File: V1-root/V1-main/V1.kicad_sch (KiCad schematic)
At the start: 214 parts, among them J17 OLED, Q1 PMOS, SW1 SW_SPST, U1 AP64500SP-3.3v, U7 XIAO-ESP32-S3-DIP_ui, Y1 Crystal_GND24

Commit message: 回路図とフットプリント終わった
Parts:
- removed J?: debug_STM, symbol Connector:Conn_01x09_Socket
- added J3: DebugSTM, Connector_PinSocket_2.54mm:PinSocket_1x07_P2.54mm_Vertical, symbol Connector:Conn_01x07_Socket
- BZ1: renamed from BZ?; footprint (none) -> Buzzer_Beeper:Buzzer_Murata_PKLCS1212E
- C1: footprint 74th:Capacitor_0402_1005 -> Capacitor_SMD:C_0603_1608Metric_Pad1.08x0.95mm_HandSolder
- C12, C18: renamed from C?; value C -> 4.7; footprint (none) -> Capacitor_SMD:C_0805_2012Metric_Pad1.18x1.45mm_HandSolder
- C13, C14, C15, C16, C17, C19, C20, C21, C22, C24, C25: renamed from C?; value C -> 0.1; footprint (none) -> Capacitor_SMD:C_0603_1608Metric_Pad1.08x0.95mm_HandSolder
- C23: renamed from C?; value C -> 1; footprint (none) -> Capacitor_SMD:C_0805_2012Metric_Pad1.18x1.45mm_HandSolder
- C26, C28, C39, C40, C45, C46, C53, C54: renamed from C?; footprint (none) -> Capacitor_SMD:C_0805_2012Metric_Pad1.18x1.45mm_HandSolder
- C27, C29, C31, C32, C41, C42, C43, C44, C47, C48, C49, C50, C55, C56, C57: renamed from C?; footprint (none) -> Capacitor_SMD:C_0603_1608Metric_Pad1.08x0.95mm_HandSolder
- C30: renamed from C20; footprint Capacitor_SMD:C_Elec_4x5.4 -> Capacitor_SMD:C_0805_2012Metric_Pad1.18x1.45mm_HandSolder
- C34: renamed from C?; footprint Capacitor_SMD:C_Elec_4x5.4 -> Capacitor_SMD:C_0805_2012Metric_Pad1.18x1.45mm_HandSolder
- C35: renamed from C16; value 10p -> 6.8p
- C36: renamed from C17; value 10p -> 6.8p
- C37, C38: renamed from C?; value 10p -> 6.8p
- C51, C52: renamed from C?; footprint (none) -> Capacitor_SMD:CP_Elec_6.3x5.9
- C9: renamed from C?; footprint Capacitor_SMD:C_0402_1005Metric -> Capacitor_SMD:C_0603_1608Metric_Pad1.08x0.95mm_HandSolder
- FB1, FB2: renamed from FB?; footprint (none) -> Resistor_SMD:R_0603_1608Metric_Pad0.98x0.95mm_HandSolder
- J2: renamed from J?; footprint (none) -> Connector_JST:JST_XH_S3B-XH-A_1x03_P2.50mm_Horizontal
- NT1, NT2, NT3, NT4: renamed from NT?; footprint (none) -> NetTie:NetTie-2_THT_Pad1.0mm
- Q10, Q11, Q4, Q5, Q6, Q7, Q8, Q9: renamed from Q?; footprint (none) -> Package_TO_SOT_SMD:LFPAK56
- R1: renamed from R?; footprint (none) -> Resistor_SMD:R_0603_1608Metric
- R48, R49, R50, R51, R52, R53, R54, R55, R56, R57, R58, R59, R60, R61, R62, R63: renamed from R?; footprint (none) -> Resistor_SMD:R_0603_1608Metric_Pad0.98x0.95mm_HandSolder
- R64, R65: renamed from R?; footprint (none) -> FC4L110R005FER:FC4L110_OHM
- U10, U11, U18, U19: renamed from U?; footprint DRM8_3P38X2P45_TEX -> UCC27211ADRMR:DRM8_3P38X2P45_TEX
- U21, U22: renamed from U?; footprint (none) -> 74HC4053PW:SOT403-1_NXP
- Y1: footprint Crystal:Crystal_SMD_3225-4Pin_3.2x2.5mm -> ABM8W-16.0000MHZ-8-K1Z-T3:XTAL4P_ABM8W_ABR
- Y2: renamed from Y?; footprint Crystal:Crystal_SMD_3225-4Pin_3.2x2.5mm -> ABM8W-16.0000MHZ-8-K1Z-T3:XTAL4P_ABM8W_ABR
- gave numbers to parts that had none: 81
- renumbered C5 to C10, C6 to C11, C21 to C2, C8 to C33, C18 to C4, C2 to C5, C3 to C6, C4 to C7, D2 to D14, J17 to J1, R6 to R10, R87 to R11, R88 to R18, R8 to R19, R3 to R47, R12 to R6, R13 to R7, R89 to R9, U7 to U20, U1 to U4, slide to slide1
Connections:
- net mainRX4→uiTX is gone; now on net mRXcTX: U20.7 (PB08_A6_D6_TX)
- net mainTX4→uiRX is gone; now on net mTXcRX: U20.8 (PB09_A7_D7_RX)
- net +3.3V: now also J3.1 (Pin_1)
- net GND: now also J3.4 (Pin_4)
- net NRST: now also J3.5 (Pin_5)
- net RXlinkTX: now also J3.6 (Pin_6)
- net SWD_CLK: now also J3.3 (Pin_3)
- net SWD_IO: now also J3.2 (Pin_2)
- net TXlinkRX: now also J3.7 (Pin_7)
- net SPI_CS: now reaches U2.34 (PA12)
- net SPI_CS: now also U3.51 (PA15)
- net SPI_MISO: now reaches U2.41 (PB4)
- net SPI_MISO: now also U3.57 (PB4)
- net SPI_MOSI: now reaches U2.42 (PB5)
- net SPI_MOSI: now also U3.58 (PB5)
- net SWO: no longer names the net of U21.4 (Z)
- net mSWO: no longer names the net of U21.5 (Z0)
- net mSWO: no longer U3.56 (PB3)
- net sSWO: no longer names the net of U21.3 (Z1)
- net sSWO: no longer U2.40 (PB3)
- new net SPI_SCK: U2.40 (PB3), U3.56 (PB3)

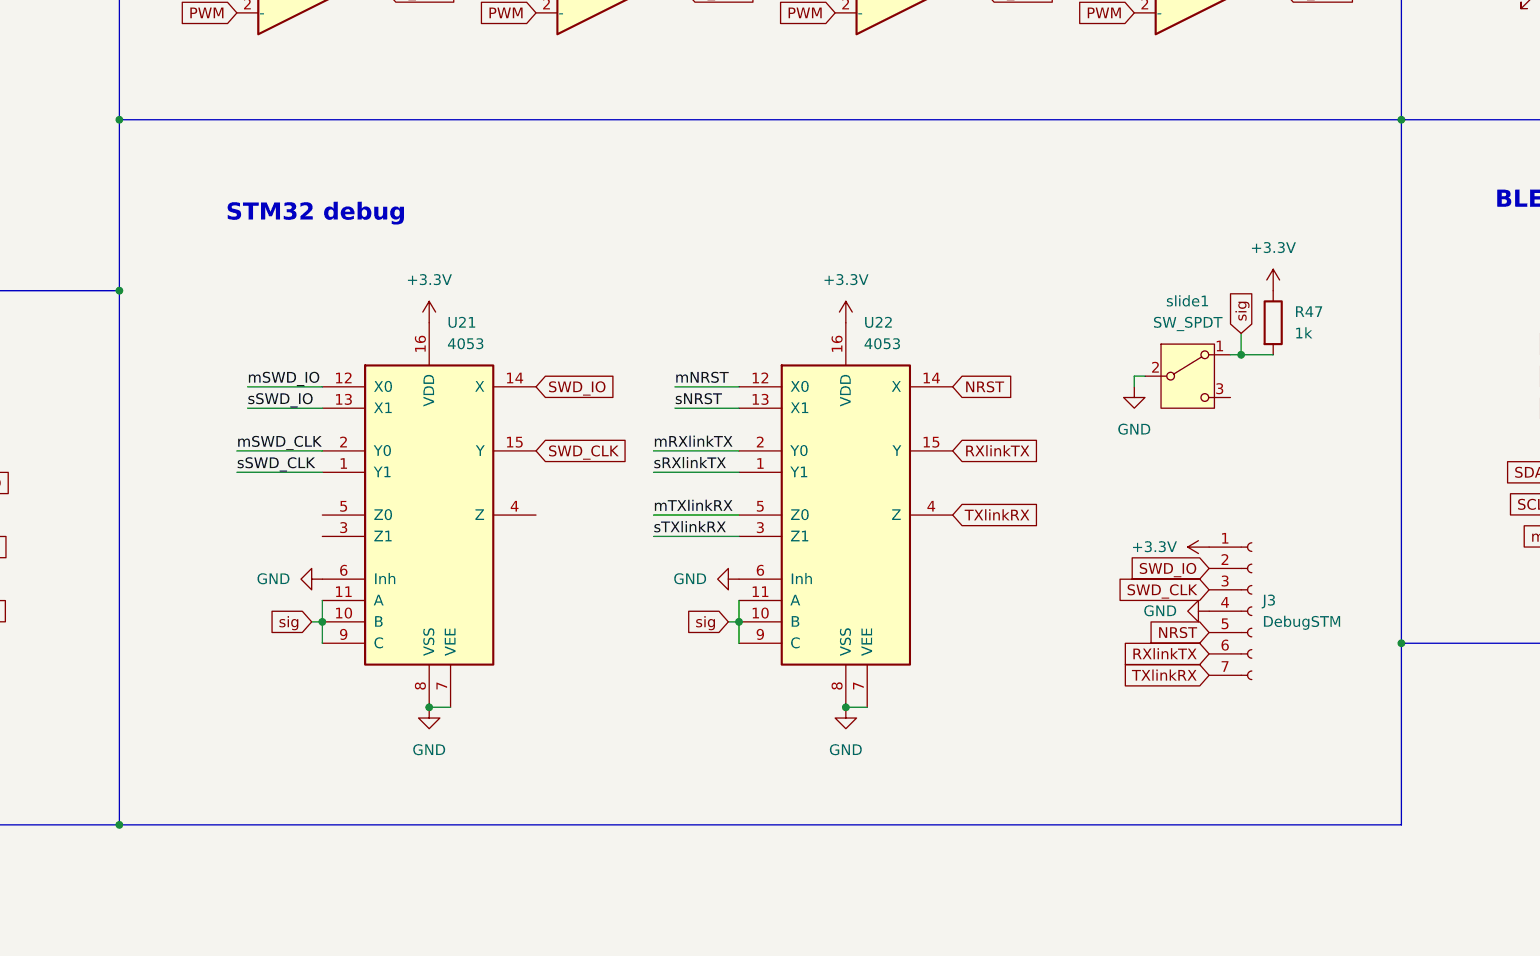
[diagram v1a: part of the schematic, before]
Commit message: UART/SWD&MCU切り替え追加
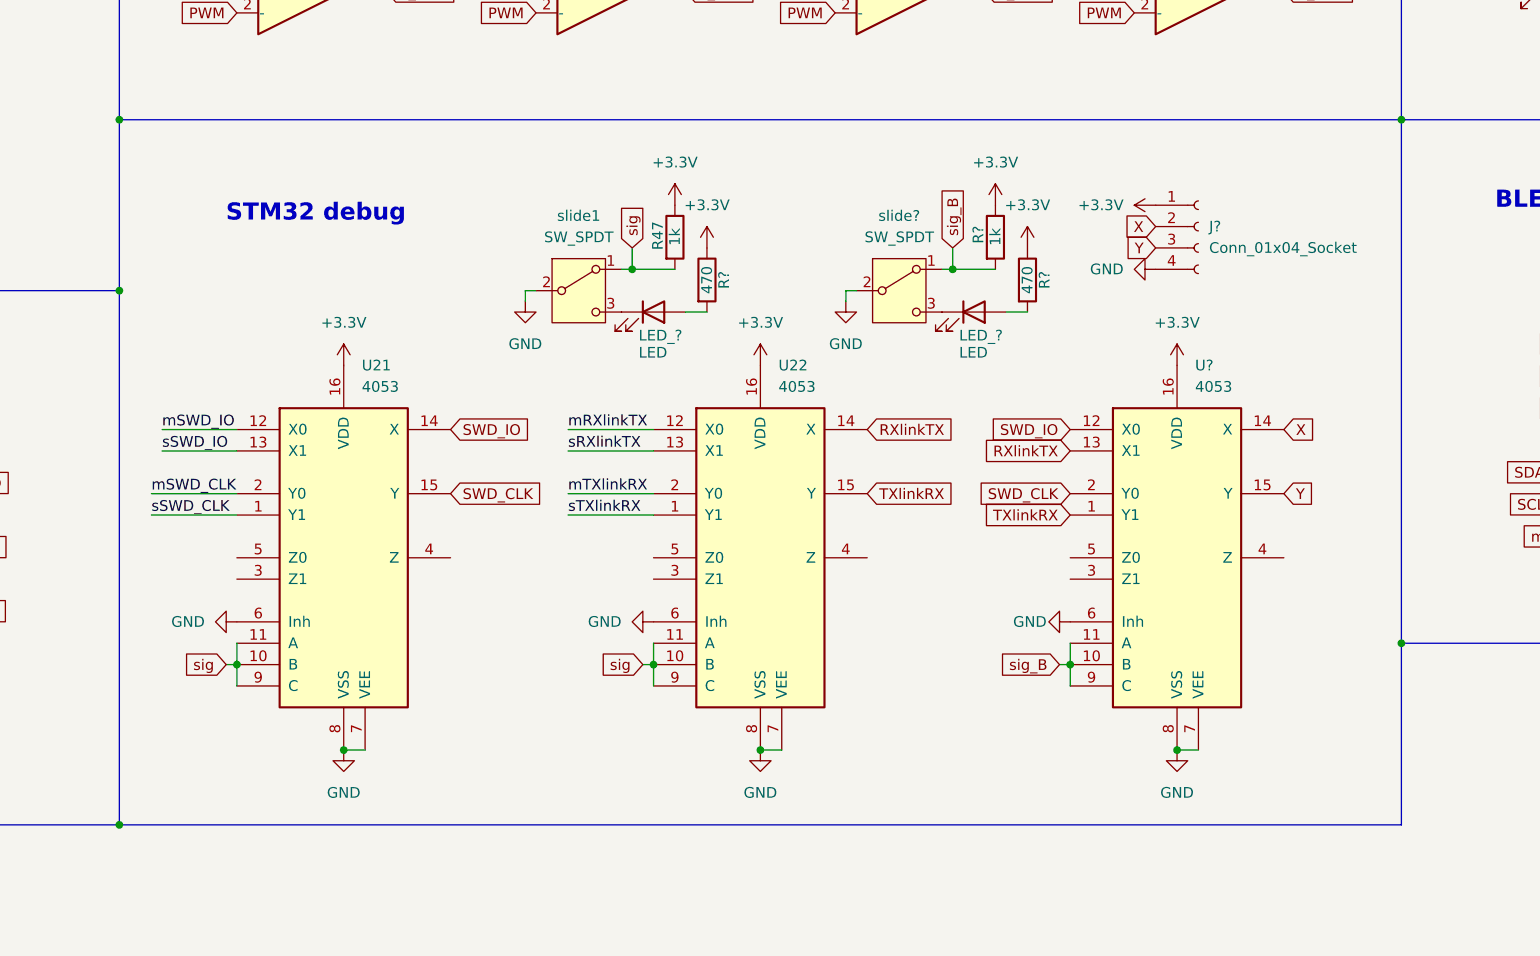
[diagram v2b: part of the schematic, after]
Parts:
- removed J3: DebugSTM, Connector_PinSocket_2.54mm:PinSocket_1x07_P2.54mm_Vertical, symbol Connector:Conn_01x07_Socket
- added J?: Conn_01x04_Socket, symbol Connector:Conn_01x04_Socket
- added LED_? (x2): LED, LED_SMD:LED_0603_1608Metric_Pad1.05x0.95mm_HandSolder, symbol Device:LED
- added R? (x2): 470, Resistor_SMD:R_0603_1608Metric, symbol Device:R
- added R?: 1k, Resistor_THT:R_Axial_DIN0207_L6.3mm_D2.5mm_P10.16mm_Horizontal, symbol Device:R
- added U?: 4053, 74HC4053PW:SOT403-1_NXP, symbol 4xxx:4053
- added slide?: SW_SPDT, Connector_PinSocket_2.54mm:PinSocket_1x03_P2.54mm_Vertical, symbol Switch:SW_SPDT
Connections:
- net NRST is gone; now on net RXlinkTX: U22.14 (X)
- net +3.3V: now also J?.1 (Pin_1), R?.1, R?.1, R?.1, U?.16 (VDD)
- net GND: now also J?.4 (Pin_4), U?.6 (Inh), U?.7 (VEE), U?.8 (VSS), slide?.2 (B)
- net RXlinkTX: now also U?.13 (X1); no longer U22.15 (Y)
- net SWD_CLK: now also U?.2 (Y0)
- net SWD_IO: now also U?.12 (X0)
- net TXlinkRX: now also U22.15 (Y), U?.1 (Y1); no longer U22.4 (Z)
- net mNRST: no longer U22.12 (X0)
- net mRXlinkTX: now also U22.12 (X0); no longer U22.2 (Y0)
- net mTXlinkRX: now also U22.2 (Y0); no longer U22.5 (Z0)
- net sNRST: no longer U22.13 (X1)
- net sRXlinkTX: now also U22.13 (X1); no longer U22.1 (Y1)
- net sTXlinkRX: now also U22.1 (Y1); no longer U22.3 (Z1)
- net at slide1.3 (C): now also LED_?.1 (K)
- new net: LED_?.2 (A), R?.2 (x2)
- new net: LED_?.1 (K), slide?.3 (C)
- new net X: J?.2 (Pin_2), U?.14 (X)
- new net Y: J?.3 (Pin_3), U?.15 (Y)
- new net sig_B: R?.2, U?.10 (B), U?.11 (A), U?.9 (C), slide?.1 (A)
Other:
- moved on the sheet: R47, U21, U22, slide1

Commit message: reset&memoryつけましter
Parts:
- removed C55: 0.1, Capacitor_SMD:C_0603_1608Metric_Pad1.08x0.95mm_HandSolder, symbol Device:C_Small
- removed D14: D_Schottky, Diode_THT:D_A-405_P10.16mm_Horizontal, symbol Device:D_Schottky
- removed U20: XIAO-ESP32-S3-DIP_ui, Seeed Xiao:XIAO-ESP32-S3-DIP, symbol Seeed_Xiao:XIAO-ESP32-S3-DIP
- removed tact_3: SW_Push, Button_Switch_THT:SW_PUSH-12mm, symbol Switch:SW_Push
- added C?: 0.1, symbol Device:C_Small
- added R?: 1k, Resistor_THT:R_Axial_DIN0207_L6.3mm_D2.5mm_P10.16mm_Horizontal, symbol Device:R
- added U?: AT25SF321B-SSHB-B, AT25SF321B-SSHB-B:SOIC127P599X175-8N, symbol AT25SF321B-SSHB:AT25SF321B-SSHB-B
- added tact_? (x2): SW_Push, Button_Switch_THT:SW_PUSH-12mm, symbol Switch:SW_Push
- added togg?: SW_SPDT, Connector_PinSocket_2.54mm:PinSocket_1x03_P2.54mm_Vertical, symbol Switch:SW_SPDT
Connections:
- net +3.3V: now also C?.1, R?.1, U?.3 (~{WP}), U?.7 (~{HOLD}), U?.8 (VCC)
- net Buzzer: now also U3.24 (PB0)
- net GND: now also C?.2, U?.4 (GND), tact_?.2, tact_?.2, togg?.2 (B)
- net SPI_MISO: now also U?.2 (SO(I/O1))
- net SPI_MOSI: now also U?.5 (SI(I/O0))
- net SPI_SCK: now also U?.6 (SCK)
- net mNRST: now also tact_?.1
- net sNRST: now also tact_?.1
- net start: now also U3.54 (PC12)
- net tact_1: now also U3.3 (PC14)
- net tact_2: now also U3.4 (PC15)
- net slide: now reaches U3.2 (PC13)
- net slide: now also R?.2, togg?.1 (A)
- net SPI_CS_FLASH: now reaches U3.34 (PB12)
- net SPI_CS_FLASH: now also U?.1 (~{CS})
- net SPI_CS renamed SPI_CS_MCU
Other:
- note added: "SPI FLASH"
- note removed: "BLESUB XIAO ESP32S3"
- moved on the sheet: C4, J1, R8, tact_1, tact_2, togg1

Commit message: footprint紐付け&pcb同期
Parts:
- C57: renamed from C?; footprint (none) -> Capacitor_SMD:C_0603_1608Metric_Pad1.08x0.95mm_HandSolder
- J3: renamed from J?; footprint (none) -> Connector_PinSocket_2.54mm:PinSocket_1x04_P2.54mm_Vertical
- U20: renamed from U?; footprint AT25SF321B-SSHB-B:SOIC127P599X175-8N -> AT25SF321B-SSHB:SOIC127P599X175-8N
- tact_1, tact_2: footprint Button_Switch_THT:SW_PUSH-12mm -> Button_Switch_THT:SW_TH_Tactile_Omron_B3F-10xx
- tact_3, tact_4: renamed from tact_?; footprint Button_Switch_THT:SW_PUSH-12mm -> 74th:Switch_SKRPABE010
- gave numbers to parts that had none: 9
- renumbered C56 to C55, C57 to C56, R9 to R10, R10 to R11, R11 to R12, R12 to R13, R13 to R14, R14 to R15, R15 to R16, R16 to R17, R17 to R18, R18 to R19, R19 to R20, R20 to R21, R21 to R22, R22 to R23, R23 to R24, R24 to R25, R25 to R26, R26 to R27, R27 to R28, R28 to R29, R29 to R30, R30 to R31, R31 to R32, R32 to R33, R33 to R34, R34 to R35, R35 to R36, R36 to R37, R37 to R38, R38 to R39, R39 to R40, R40 to R41, R41 to R42, R42 to R43, R43 to R44, R44 to R45, R45 to R46, R46 to R47, R47 to R48, R48 to R52, R49 to R53, R50 to R54, R51 to R55, R52 to R56, R53 to R57, R54 to R58, R55 to R59, R56 to R60, R57 to R61, R58 to R62, R59 to R63, R60 to R64, R61 to R65, R62 to R66, R63 to R67, R64 to R68, R65 to R69, R8 to R9, togg1 to togg2

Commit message: sideLine配線&MD系配置終了
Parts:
- removed SW1: SW_SPST, Connector_PinSocket_2.54mm:PinSocket_1x02_P2.54mm_Vertical, symbol Switch:SW_SPST
- removed U4, U5, U6, U7, U8, U9: LM393, Package_SO:SOIC-8_3.9x4.9mm_P1.27mm, symbol Comparator:LM393
- added unit 2 of U12
- added unit 3 of U12
- added unit 2 of U13
- added unit 3 of U13
- added unit 2 of U14
- added unit 3 of U14
- added unit 2 of U15
- added unit 3 of U15
- added unit 3 of U16
- added unit 2 of U16
- added unit 2 of U17
- added unit 3 of U17
- added slidemain1: SW_SPDT, 74th:SLIDE_akiduki, symbol Switch:SW_SPDT
- C10: footprint Capacitor_SMD:CP_Elec_4x5.4 -> Capacitor_SMD:C_0603_1608Metric_Pad1.08x0.95mm_HandSolder
- C11: footprint Capacitor_SMD:CP_Elec_5x5.7 -> Capacitor_SMD:C_1206_3216Metric
- C5, C6, C7: footprint Capacitor_SMD:CP_Elec_5x5.4 -> Capacitor_SMD:C_0805_2012Metric
- slide1, slide2, togg1, togg2: footprint Connector_PinSocket_2.54mm:PinSocket_1x03_P2.54mm_Vertical -> 74th:SLIDE_akiduki
- renumbered U22 to U10, U23 to U11, U10 to U4, U11 to U5, U18 to U6, U19 to U7, U20 to U8, U21 to U9
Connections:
- net +3.3V: now also U12.8 (V+), U13.8 (V+), U14.8 (V+), U15.8 (V+), U16.8 (V+), U17.8 (V+)
- net A_mark: now also U12.1
- net B_goal: now also U14.7; no longer U15.1
- net B_mark: now also U12.7
- net C_goal: now also U15.1; no longer U16.1
- net C_mark: now also U13.1; no longer U12.1
- net D_goal: now also U15.7; no longer U17.1
- net D_mark: now also U13.7; no longer U13.1
- net ENCORDER_PWM: now also U16.2 (-), U17.2 (-), U16.6 (-), U17.6 (-)
- net GND: now also U12.4 (V-), U13.4 (V-), U14.4 (V-), U15.4 (V-), U16.4 (V-), U16.5 (+), U17.4 (V-), U17.5 (+), slidemain1.2 (B)
- net PWM: now also U12.6 (-), U13.6 (-), U14.6 (-), U15.6 (-); no longer U16.2 (-), U17.2 (-)
- net encorderADC_L: now also U17.3 (+)
- net encorderADC_R: now also U16.3 (+)
- net encorderDigi_L: now also U17.1
- net encorderDigi_R: now also U16.1
- net goal_B: now also U14.5 (+); no longer U15.3 (+)
- net goal_C: now also U15.3 (+); no longer U16.3 (+)
- net goal_D: now also U15.5 (+); no longer U17.3 (+)
- net mark_A: now also U12.3 (+)
- net mark_B: now also U12.5 (+)
- net mark_C: now also U13.3 (+); no longer U12.3 (+)
- net mark_D: now also U13.5 (+); no longer U13.3 (+)
- net at Q1.1 (G), R1.1: now also slidemain1.1 (A)
- net at R30.1: now also U17.7
- net at R23.1: now also U16.7
